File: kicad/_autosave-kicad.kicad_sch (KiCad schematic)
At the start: 22 parts, among them SW1 SW_Push, SW10 SW_Push, SW11 SW_Push, SW12 SW_Push, SW13 SW_Push, SW15 SW_Push, SW16 SW_Push, SW17 SW_Push, SW2 SW_Push, SW3 SW_Push, SW4 SW_Push, SW5 SW_Push, SW6 SW_Push, SW7 SW_Push, SW8 SW_Push, SW9 SW_Push

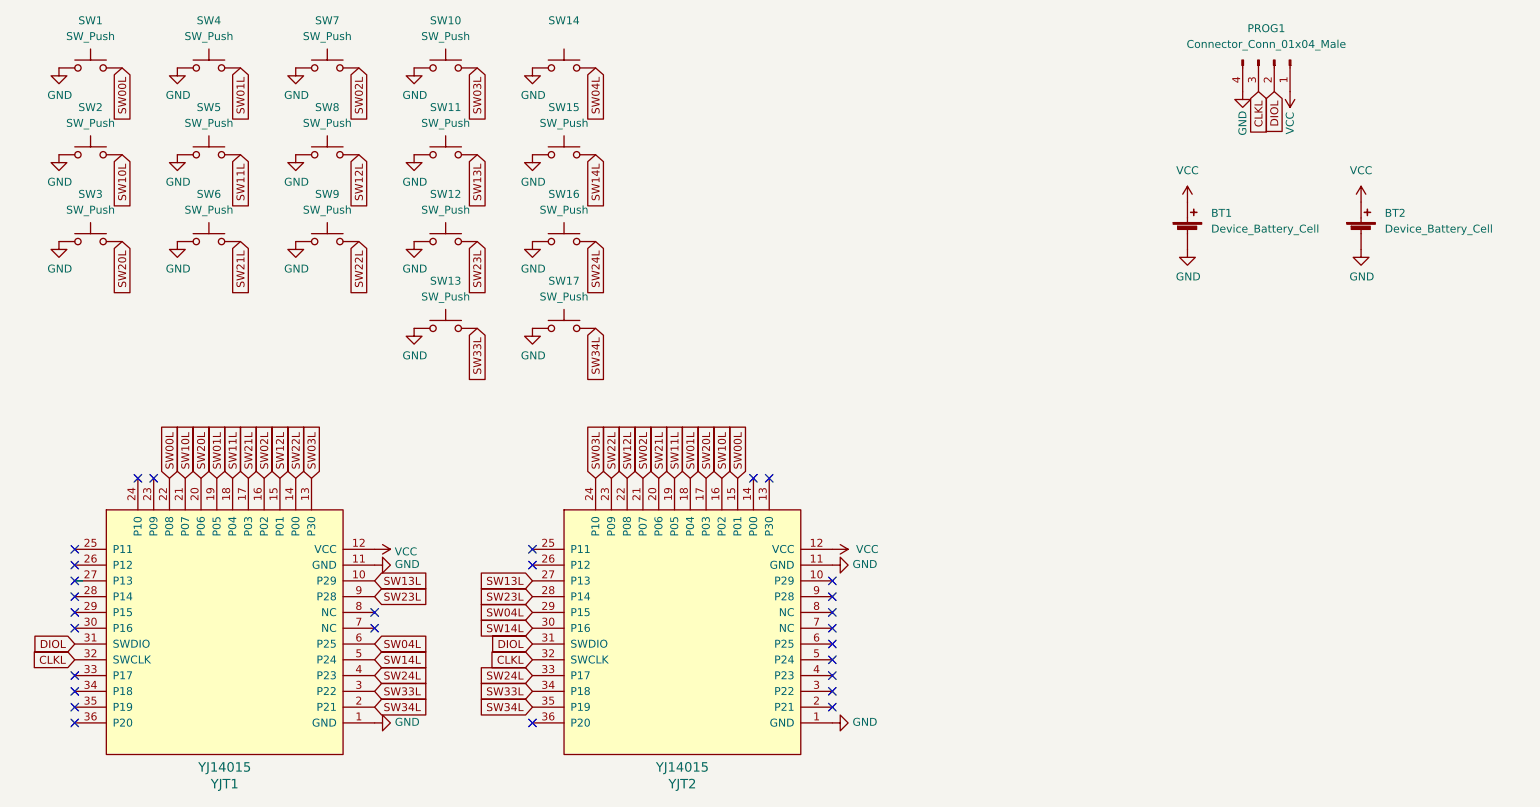
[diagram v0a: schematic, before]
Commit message: fixed schema and drew traces
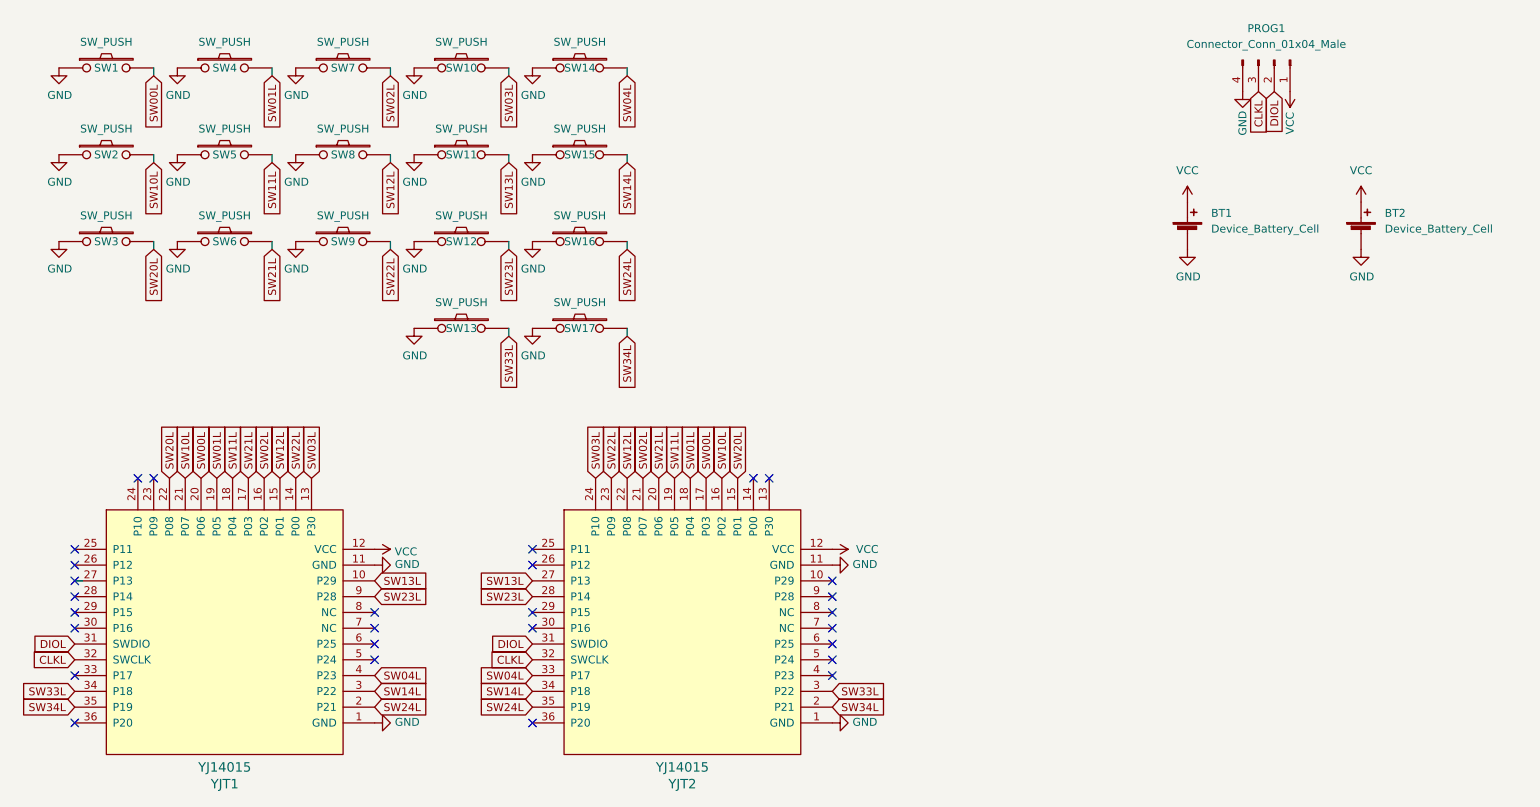
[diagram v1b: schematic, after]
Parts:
- removed SW1, SW10, SW11, SW12, SW13, SW15, SW16, SW17, SW2, SW3, SW4, SW5, SW6, SW7, SW8, SW9: SW_Push, symbol Switch:SW_Push
- removed SW14: (no value), symbol Switch:SW_Push
- added SW1, SW10, SW11, SW12, SW13, SW14, SW15, SW16, SW17, SW2, SW3, SW4, SW5, SW6, SW7, SW8, SW9: SW_PUSH, gurt-portable:Choc_PG1350_Choc_Spacing_Reversible, symbol pierce:SW_PUSH
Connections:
- net GND: now also SW1.1, SW10.1, SW11.1, SW12.1, SW13.1, SW14.1, SW15.1, SW16.1, SW17.1, SW2.1, SW3.1, SW4.1, SW5.1, SW6.1, SW7.1, SW8.1, SW9.1
- net SW00L: now also YJT1.20 (P06), YJT2.17 (P03), SW1.2; no longer YJT1.22 (P08), YJT2.15 (P01)
- net SW01L: now also SW4.2
- net SW02L: now also SW7.2
- net SW03L: now also SW10.2
- net SW04L: now also YJT1.4 (P23), YJT2.33 (P17), SW14.2; no longer YJT1.6 (P25), YJT2.29 (P15)
- net SW10L: now also SW2.2
- net SW11L: now also SW5.2
- net SW12L: now also SW8.2
- net SW13L: now also SW11.2
- net SW14L: now also YJT1.3 (P22), YJT2.34 (P18), SW15.2; no longer YJT1.5 (P24), YJT2.30 (P16)
- net SW20L: now also YJT1.22 (P08), YJT2.15 (P01), SW3.2; no longer YJT1.20 (P06), YJT2.17 (P03)
- net SW21L: now also SW6.2
- net SW22L: now also SW9.2
- net SW23L: now also SW12.2
- net SW24L: now also YJT1.2 (P21), YJT2.35 (P19), SW16.2; no longer YJT1.4 (P23), YJT2.33 (P17)
- net SW33L: now also YJT1.34 (P18), YJT2.3 (P22), SW13.2; no longer YJT1.3 (P22), YJT2.34 (P18)
- net SW34L: now also YJT1.35 (P19), YJT2.2 (P21), SW17.2; no longer YJT1.2 (P21), YJT2.35 (P19)
